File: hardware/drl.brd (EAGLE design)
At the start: 56.5 x 32.4 mm, 27 parts, among them IC1 TINY13-20SU, Q1 IRF3205, Q2 IRF3205, T1 BC817-40, X1 CON1, X2 CON2

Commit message: Small editions in schematic and board design.
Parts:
- D1, D2: value (none) -> LL4148
- IC2: value (none) -> 5V
- S1: value (none) -> MODE
- moved X2 0.32 mm to (33.0, 5.40)
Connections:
- net N$7 renamed LOW_BEAM_IN
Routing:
- net N$2: track 0.16 -> 2.81 mm
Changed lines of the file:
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@@
 <attribute name="OC_FARNELL" value="unknown" x="43.18" y="5.3975" size="1.778" layer="27" rot="R180" display="off"/>
 </element>
-<element name="X2" library="con-wago-500" package="W237-102" value="CON2" x="32.7025" y="5.3975" rot="R180">
-<attribute name="OC_NEWARK" value="70K9898" x="32.7025" y="5.3975" size="1.778" layer="27" rot="R180" display="off"/>
-<attribute name="MPN" value="237-102" x="32.7025" y="5.3975" size="1.778" layer="27" rot="R180" display="off"/>
-<attribute name="MF" value="" x="32.7025" y="5.3975" size="1.778" layer="27" rot="R180" display="off"/>
-<attribute name="OC_FARNELL" value="unknown" x="32.7025" y="5.3975" size="1.778" layer="27" rot="R180" display="off"/>
+<element name="X2" library="con-wago-500" package="W237-102" value="CON2" x="33.02" y="5.3975" rot="R180">
+<attribute name="OC_NEWARK" value="70K9898" x="33.02" y="5.3975" size="1.778" layer="27" rot="R180" display="off"/>
+<attribute name="MPN" value="237-102" x="33.02" y="5.3975" size="1.778" layer="27" rot="R180" display="off"/>
+<attribute name="MF" value="" x="33.02" y="5.3975" size="1.778" layer="27" rot="R180" display="off"/>
+<attribute name="OC_FARNELL" value="unknown" x="33.02" y="5.3975" size="1.778" layer="27" rot="R180" display="off"/>
 </element>
 <element name="R2" library="rcl" package="0204/7" value="1k" x="24.765" y="21.2725"/>
-<element name="D1" library="semicon-smd-ipc" package="SOD80" value="" x="15.5575" y="3.81" rot="MR180"/>
+<element name="D1" library="semicon-smd-ipc" package="SOD80" value="LL4148" x="15.5575" y="3.81" rot="MR180"/>
 <element name="R5" library="rcl" package="R0805" value="10k" x="18.415" y="20.32" rot="MR270"/>
 <element name="Q1" library="my_stuff" package="TO220BV" value="IRF3205" x="42.8625" y="23.1775"/>
 <element name="Q2" library="my_stuff" package="TO220BV" value="IRF3205" x="42.8625" y="16.51"/>
-<element name="IC2" library="my_stuff" package="SOIC8" value="" x="10.4775" y="15.5575" rot="MR180"/>
+<element name="IC2" library="my_stuff" package="SOIC8" value="5V" x="10.4775" y="15.5575" rot="MR180"/>
 <element name="C3" library="rcl" package="SMC_D" value="10u" x="10.16" y="6.6675" rot="MR90"/>
 <element name="C4" library="rcl" package="SMC_D" value="10u" x="18.0975" y="10.795" rot="MR270"/>
-<element name="D2" library="semicon-smd-ipc" package="SOD80" value="" x="35.56" y="11.1125" rot="MR270"/>
+<element name="D2" library="semicon-smd-ipc" package="SOD80" value="LL4148" x="35.56" y="11.1125" rot="MR270"/>
 <element name="C5" library="resistor" package="C0805K" value="100n" x="33.02" y="17.78" rot="MR90"/>
 <element name="R8" library="rcl" package="R0805" value="10k" x="29.845" y="24.765" rot="MR270"/>
@@
 <element name="C6" library="resistor" package="C0805K" value="100n" x="32.385" y="24.765" rot="MR270"/>
 <element name="R10" library="rcl" package="R0805" value="10k" x="7.3025" y="21.59" rot="MR90"/>
-<element name="S1" library="switch-omron" package="B3F-10XX" value="" x="25.4" y="16.51" rot="R180">
+<element name="S1" library="switch-omron" package="B3F-10XX" value="MODE" x="25.4" y="16.51" rot="R180">
 <attribute name="OC_NEWARK" value="36M3542" x="25.4" y="16.51" size="1.778" layer="27" rot="R180" display="off"/>
 <attribute name="MPN" value="B3F-1000" x="25.4" y="16.51" size="1.778" layer="27" rot="R180" display="off"/>
@@
 <polygon width="0.4064" layer="16" isolate="0.8128">
 <vertex x="0" y="0"/>
-<vertex x="56.515" y="0.3175"/>
+<vertex x="56.515" y="0"/>
 <vertex x="56.515" y="32.385"/>
 <vertex x="0" y="32.385"/>
@@
 <wire x1="13.97" y1="12.7" x2="13.97" y2="19.685" width="0.4064" layer="1"/>
 <via x="13.97" y="19.685" extent="1-16" drill="0.6"/>
-<wire x1="26.035" y1="15.24" x2="22.1488" y2="14.2494" width="0" layer="19" extent="16-16"/>
+<wire x1="22.1488" y1="14.2494" x2="26.035" y2="15.24" width="0" layer="19" extent="16-16"/>
 </signal>
 <signal name="HI_BEAM">
@@
 <contactref element="D1" pad="2"/>
 <contactref element="X2" pad="2"/>
-<wire x1="30.2025" y1="6.6675" x2="27.305" y2="6.6675" width="1.27" layer="16"/>
+<wire x1="30.52" y1="6.6675" x2="27.305" y2="6.6675" width="1.27" layer="16"/>
 <wire x1="27.305" y1="6.6675" x2="24.4475" y2="3.81" width="1.27" layer="16"/>
 <wire x1="24.4475" y1="3.81" x2="17.2575" y2="3.81" width="1.27" layer="16"/>
@@
 <contactref element="D2" pad="1"/>
 <wire x1="33.02" y1="12.7025" x2="32.91" y2="12.8125" width="0.6096" layer="16"/>
-<wire x1="33.02" y1="12.7025" x2="35.56" y2="12.8125" width="0" layer="19" extent="16-16"/>
+<wire x1="35.56" y1="12.8125" x2="33.02" y2="12.8125" width="0.6096" layer="16"/>
+<wire x1="33.02" y1="12.8125" x2="33.02" y2="12.7025" width="0.6096" layer="16"/>
 </signal>
 <signal name="N$14">
@@
 <wire x1="20.955" y1="23.8125" x2="20.955" y2="21.2725" width="0.4064" layer="16"/>
 </signal>
-<signal name="N$7">
+<signal name="LOW_BEAM_IN">
 <contactref element="D2" pad="2"/>
 <contactref element="X2" pad="1"/>
-<wire x1="35.2025" y1="6.6675" x2="35.2025" y2="9.3725" width="1.016" layer="16"/>
 <wire x1="35.2025" y1="9.3725" x2="35.56" y2="9.4125" width="1.016" layer="16"/>
+<wire x1="35.52" y1="6.6675" x2="35.56" y2="6.6675" width="0.8128" layer="16"/>
+<wire x1="35.56" y1="6.6675" x2="35.56" y2="9.4125" width="0.8128" layer="16"/>
 </signal>
 <signal name="N$12">

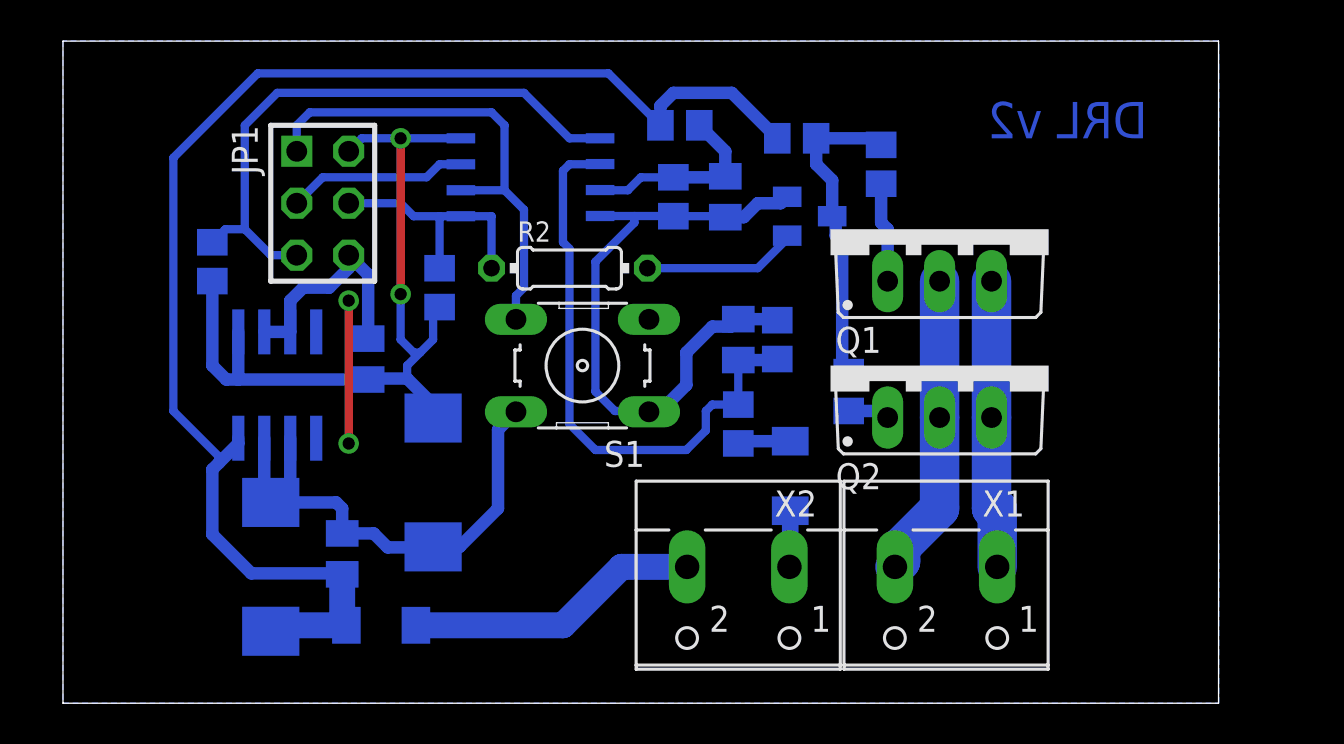
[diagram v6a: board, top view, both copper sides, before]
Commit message: The dimentions were adjusted to fit the case
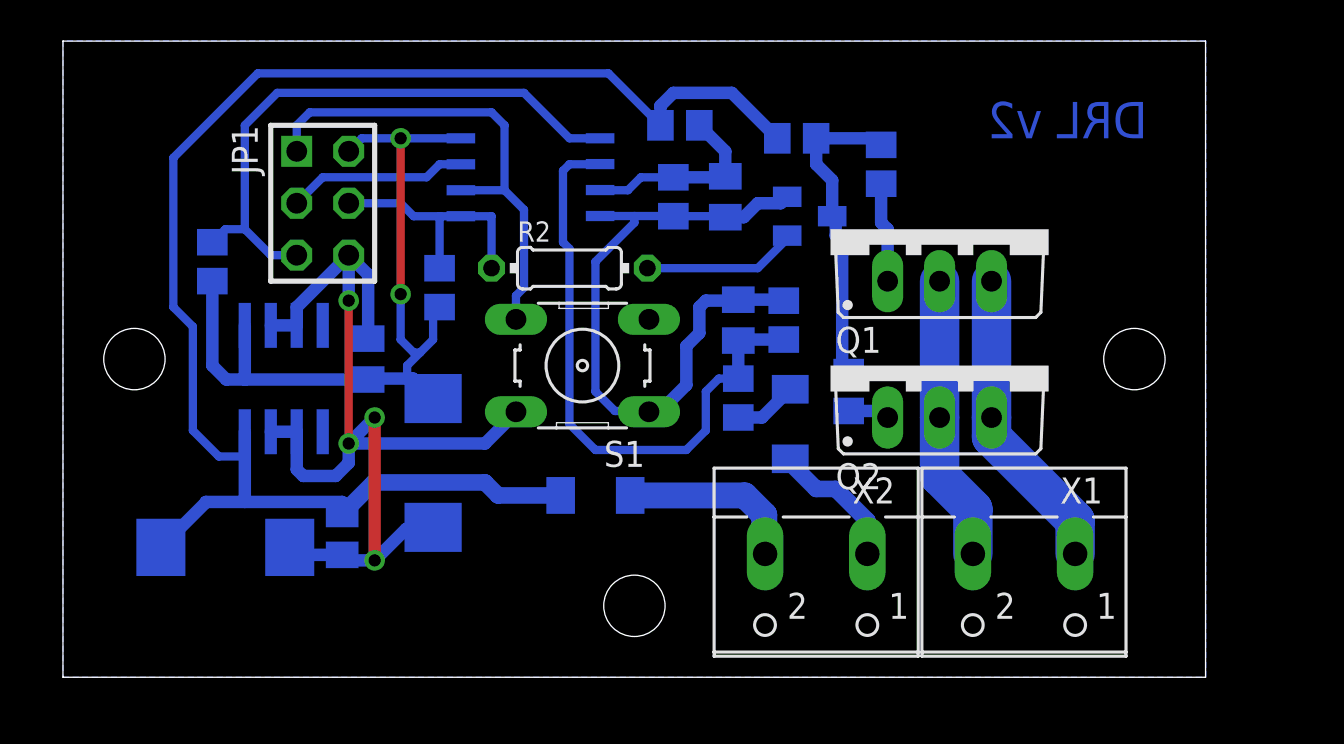
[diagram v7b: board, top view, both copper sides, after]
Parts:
- moved D1 12.3 mm to (26.0, 10.2)
- moved X1 3.86 mm to (47.0, 6.03)
- moved X2 3.86 mm to (36.8, 6.03)
- moved D2 2.54 mm to (35.6, 13.7)
- moved C3 2.42 mm to (7.94, 7.62), turned to 180 degrees
- moved R6 1.27 mm to (33.0, 14.9)
- moved R7 1.00 mm to (35.2, 18.7)
- moved C1 0.95 mm to (13.7, 8.26), turned to 270 degrees
- moved C4 0.95 mm to (18.1, 11.7)
- moved C5 0.95 mm to (33.0, 18.7)
- moved IC2 0.45 mm to (10.8, 15.9)
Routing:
- net GND: track 88.8 -> 99.8 mm, vias 2 -> 4
- net VCC12: track 69.1 -> 76.6 mm
- net +12: track 14.4 -> 8.87 mm
- net LOW_BEAM_IN: track 3.14 -> 6.80 mm
- net N$9: track 28.8 -> 29.9 mm
- net HI_BEAM: track 14.9 -> 14.0 mm
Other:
- board size 56.5 x 32.4 mm -> 55.9 x 31.1 mm
